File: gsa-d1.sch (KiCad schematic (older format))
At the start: 4 parts, among them J1 CONN-3, SW1 DPST

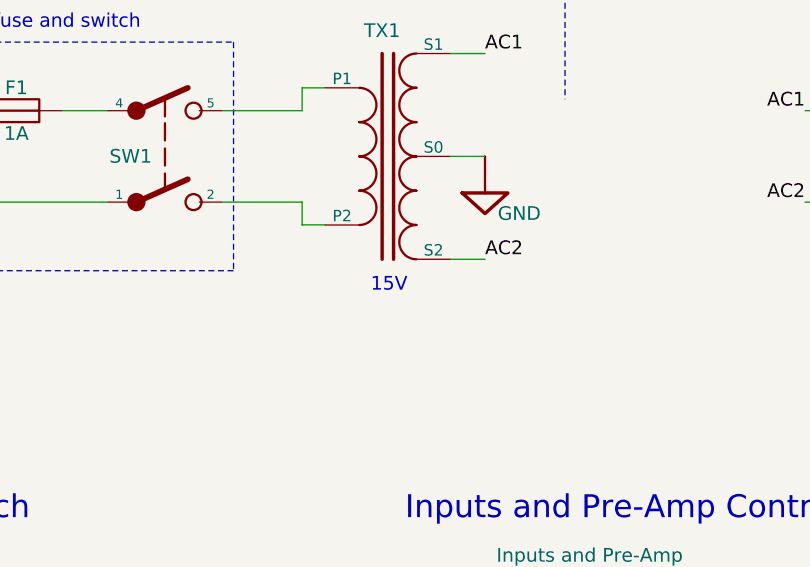
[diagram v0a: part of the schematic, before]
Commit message: Minor layout improvements to pre-amp controls
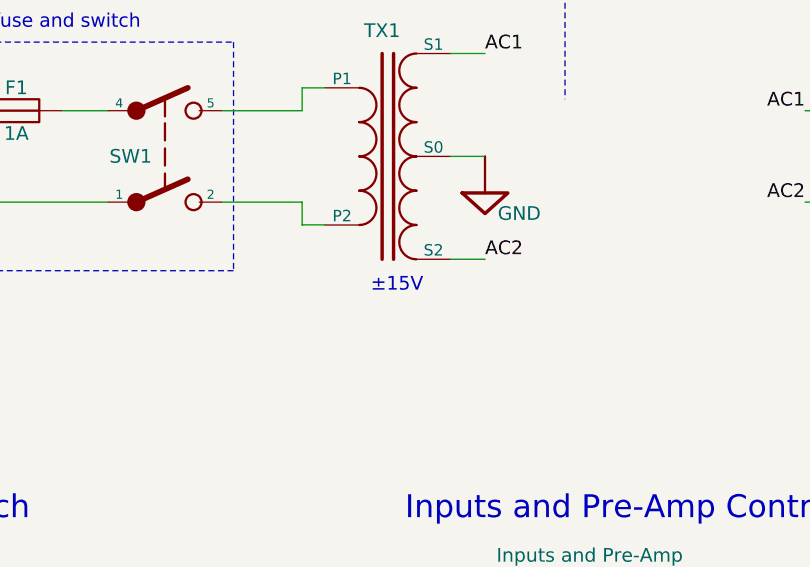
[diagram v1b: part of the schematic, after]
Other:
- note added: "±15V"
- note removed: "15V"
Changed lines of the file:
@@
 EESchema Schematic File Version 2
 LIBS:gsa
+LIBS:gsa-d1-cache
 EELAYER 25 0
 EELAYER END
@@
 AC
 Text Notes 4600 3750 0    60   ~ 0
-15V
+±15V
 $Comp
 L XFRMR-C TX1

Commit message: Updated to use KiCad v5
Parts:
- F1: footprint gsa:NONE -> (none); symbol FUSE -> gsa:FUSE
- J1: footprint gsa:NONE -> (none); symbol CONN-3 -> gsa:CONN-3
- SW1: footprint gsa:NONE -> (none); symbol DPST -> gsa:DPST
- TX1: footprint gsa:NONE -> (none); symbol XFRMR-C -> gsa:XFRMR-C
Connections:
- wire segments 22 -> 23
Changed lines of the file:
@@
-EESchema Schematic File Version 2
+EESchema Schematic File Version 4
 LIBS:gsa
 LIBS:gsa-d1-cache
-EELAYER 25 0
+EELAYER 29 0
 EELAYER END
 $Descr A4 11693 8268
@@
 Sheet 1 5
 Title "Diamond-1"
-Date "January 2018"
+Date "May 2019"
 Rev "2.0.0"
 Comp "Gemstone Amplification"
-Comment1 "© Tim Baldwin 2016,2018"
+Comment1 "© Tim Baldwin 2016,2019"
 Comment2 ""
 Comment3 ""
@@
 	1750 2900 1750 2100
 $Comp
-L CONN-3 J1
+L gsa:CONN-3 J1
 U 1 1 5A85D3B0
 P 2250 3150
 F 0 "J1" H 2250 2850 60  0000 C CNN
 F 1 "CONN-3" H 2250 2875 60  0001 C CNN
-F 2 "gsa:NONE" H 2250 3150 60  0001 C CNN
+F 2 "" H 2250 3150 60  0001 C CNN
 F 3 "" H 2250 3150 60  0000 C CNN
 	1    2250 3150
@@
 ±15V
 $Comp
-L XFRMR-C TX1
+L gsa:XFRMR-C TX1
 U 1 1 5A85D3B4
 P 4700 3150
 F 0 "TX1" H 4650 3700 60  0000 C CNN
 F 1 "XFRMR-C" H 4700 2600 60  0001 C CNN
-F 2 "gsa:NONE" H 5050 2750 60  0001 C CNN
+F 2 "" H 5050 2750 60  0001 C CNN
 F 3 "" H 5050 2750 60  0000 C CNN
 	1    4700 3150
@@
 $EndComp
 $Comp
-L DPST SW1
+L gsa:DPST SW1
 U 1 1 5A85D3B8
 P 3700 3150
 F 0 "SW1" H 3550 3150 60  0000 C CNN
 F 1 "DPST" H 3700 2850 60  0001 C CNN
-F 2 "gsa:NONE" H 3690 3340 60  0001 C CNN
+F 2 "" H 3690 3340 60  0001 C CNN
 F 3 "" H 3690 3340 60  0000 C CNN
 	1    3700 3150
@@
 $EndComp
 $Comp
-L FUSE F1
+L gsa:FUSE F1
 U 1 1 5A85D3B9
 P 3050 2950
 F 0 "F1" H 3050 3050 60  0000 C CNN
 F 1 "1A" H 3050 2850 60  0000 C CNN
-F 2 "gsa:NONE" V 3050 2950 60  0001 C CNN
+F 2 "" V 3050 2950 60  0001 C CNN
 F 3 "" V 3050 2950 60  0000 C CNN
 	1    3050 2950
@@
 	4300 2950 3950 2950
 Wire Wire Line
-	2500 3150 2500 3750
+	2500 3150 2500 3500
 Wire Wire Line
 	2650 3050 2450 3050
@@
 	5450 2100 5450 2900
 $Comp
-L GND #GND01
+L gsa:GND #GND01
 U 1 1 5A85D3CC
 P 5100 3150
@@
 $EndSheet
 $Comp
-L EARTH #GND02
+L gsa:EARTH #GND02
 U 1 1 5A86B538
 P 2500 3750
@@
 Power Supply
 $Comp
-L GND #GND?
+L gsa:GND #GND?
 U 1 1 5A9150C8
 P 2800 3750
@@
 	2800 3500 2500 3500
 Connection ~ 2500 3500
+Wire Wire Line
+	2500 3500 2500 3750
 $EndSCHEMATC

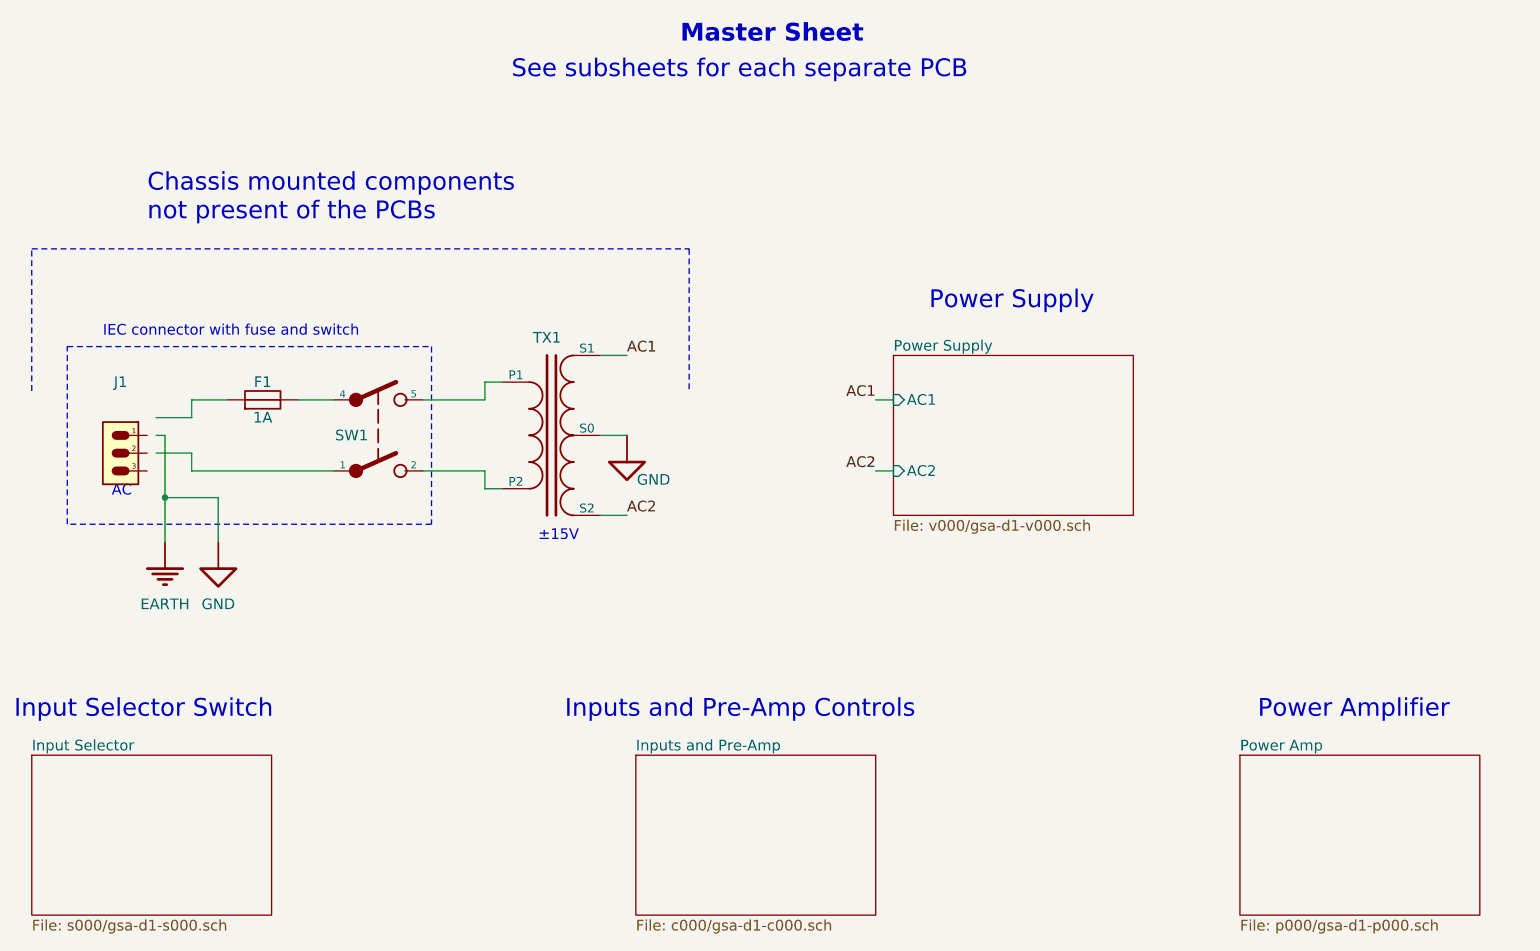
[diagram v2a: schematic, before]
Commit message: Updated to use gsa-lib v1.1
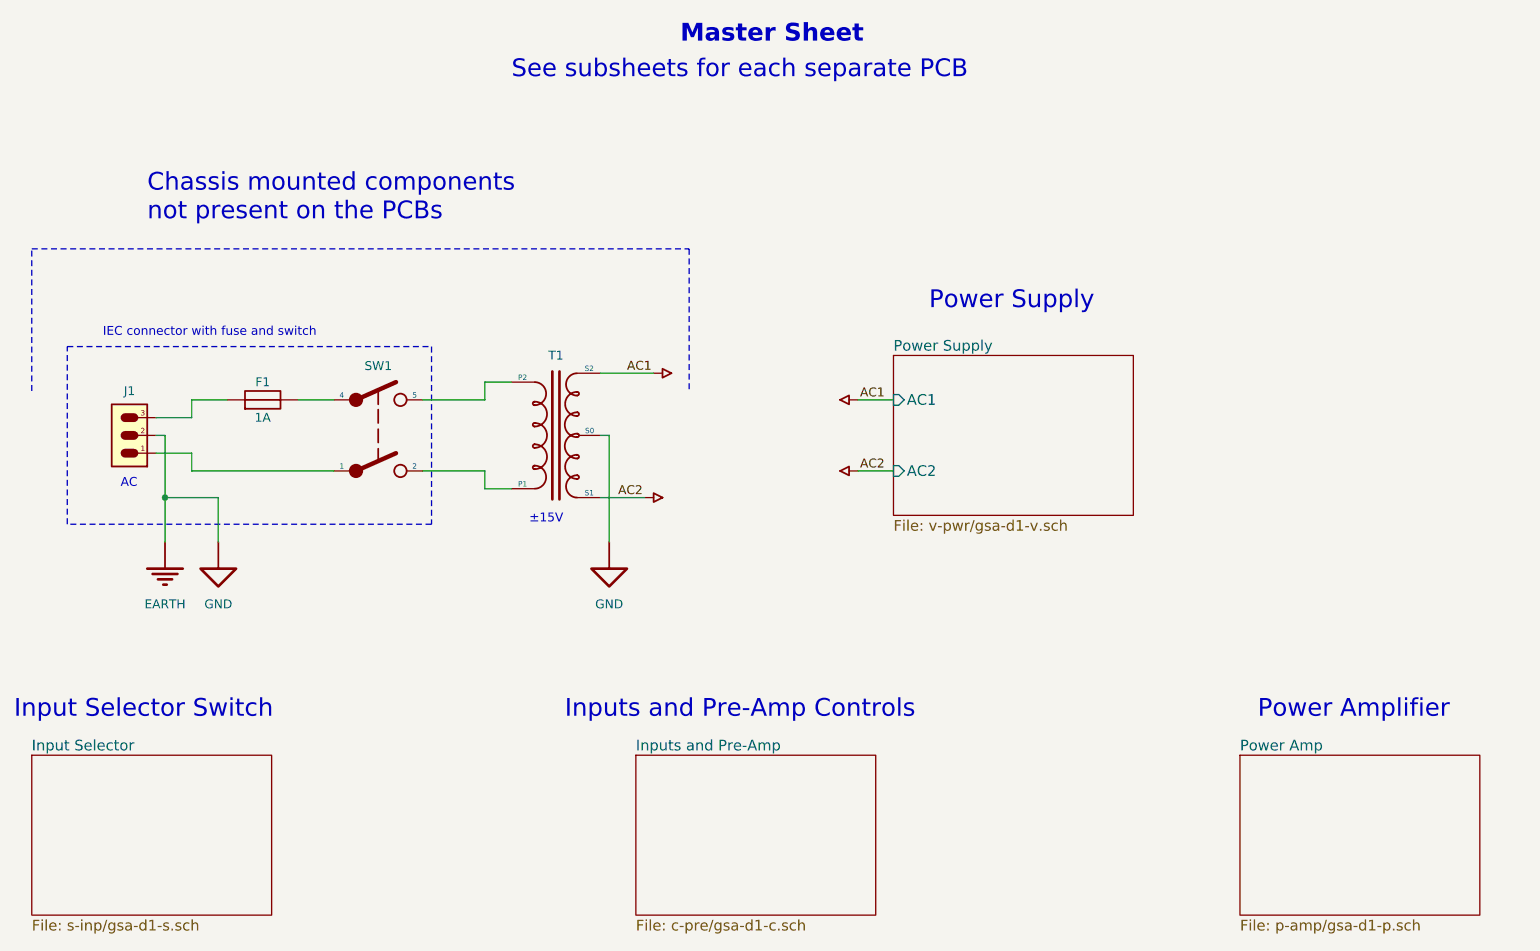
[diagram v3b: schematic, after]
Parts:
- removed SW1: DPST, symbol gsa:DPST
- removed TX1: XFRMR-C, symbol gsa:XFRMR-C
- added SW1: SW-DPST, symbol gsa:SW-DPST
- added T1: XFRMR-CTR, symbol gsa:XFRMR-CTR
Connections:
- wire segments 23 -> 24
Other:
- note added: "Chassis mounted components \nnot present on the PCBs"
- note removed: "Chassis mounted components \nnot present of the PCBs"
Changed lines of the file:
@@
 EESchema Schematic File Version 4
-LIBS:gsa
-LIBS:gsa-d1-cache
-EELAYER 29 0
+EELAYER 30 0
 EELAYER END
 $Descr A4 11693 8268
@@
 Sheet 1 5
 Title "Diamond-1"
-Date "May 2019"
-Rev "2.0.0"
+Date "May 2020"
+Rev "2.0.1"
 Comp "Gemstone Amplification"
-Comment1 "© Tim Baldwin 2016,2019"
-Comment2 ""
+Comment1 "© Tim Baldwin 2016,2020"
+Comment2 "GSA-D1-201"
 Comment3 ""
 Comment4 "Stereo Amplifier"
 $EndDescr
 Text Notes 2400 1950 0    100  ~ 0
-Chassis mounted components \nnot present of the PCBs
+Chassis mounted components \nnot present on the PCBs
 Wire Notes Line
 	1750 2900 1750 2100
-$Comp
-L gsa:CONN-3 J1
-U 1 1 5A85D3B0
-P 2250 3150
-F 0 "J1" H 2250 2850 60  0000 C CNN
-F 1 "CONN-3" H 2250 2875 60  0001 C CNN
-F 2 "" H 2250 3150 60  0001 C CNN
-F 3 "" H 2250 3150 60  0000 C CNN
-	1    2250 3150
-	-1   0    0    1
-$EndComp
-Text Notes 2200 3500 0    60   ~ 0
+Text Notes 2250 3450 0    50   ~ 0
 AC
-Text Notes 4600 3750 0    60   ~ 0
+Text Notes 4550 3650 0    50   ~ 0
 ±15V
-$Comp
-L gsa:XFRMR-C TX1
-U 1 1 5A85D3B4
-P 4700 3150
-F 0 "TX1" H 4650 3700 60  0000 C CNN
-F 1 "XFRMR-C" H 4700 2600 60  0001 C CNN
-F 2 "" H 5050 2750 60  0001 C CNN
-F 3 "" H 5050 2750 60  0000 C CNN
-	1    4700 3150
-	1    0    0    -1
-$EndComp
-$Comp
-L gsa:DPST SW1
-U 1 1 5A85D3B8
-P 3700 3150
-F 0 "SW1" H 3550 3150 60  0000 C CNN
-F 1 "DPST" H 3700 2850 60  0001 C CNN
-F 2 "" H 3690 3340 60  0001 C CNN
-F 3 "" H 3690 3340 60  0000 C CNN
-	1    3700 3150
-	1    0    0    -1
-$EndComp
 $Comp
 L gsa:FUSE F1
 U 1 1 5A85D3B9
 P 3050 2950
-F 0 "F1" H 3050 3050 60  0000 C CNN
-F 1 "1A" H 3050 2850 60  0000 C CNN
-F 2 "" V 3050 2950 60  0001 C CNN
-F 3 "" V 3050 2950 60  0000 C CNN
+F 0 "F1" H 3050 3050 50  0000 C CNN
+F 1 "1A" H 3050 2850 50  0000 C CNN
+F 2 "" V 3050 2950 50  0001 C CNN
+F 3 "" V 3050 2950 50  0001 C CNN
 	1    3050 2950
 	1    0    0    -1
 $EndComp
-Text Notes 2150 2600 0    60   ~ 0
+Text Notes 2150 2600 0    50   ~ 0
 IEC connector with fuse and switch
 Wire Wire Line
-	4950 3600 5100 3600
-Wire Wire Line
-	4950 3150 5100 3150
-Wire Wire Line
-	4950 2700 5100 2700
+	4950 3500 5200 3500
+Wire Wire Line
+	4950 2800 5250 2800
 Wire Wire Line
 	2650 3250 2650 3350
@@
 	2650 2950 2650 3050
 Wire Wire Line
-	4300 3450 4400 3450
+	4300 3450 4450 3450
 Wire Wire Line
 	4300 3350 4300 3450
@@
 	4300 2850 4300 2950
 Wire Wire Line
-	4400 2850 4300 2850
+	4450 2850 4300 2850
 Wire Notes Line
 	1750 2100 5450 2100
 Wire Notes Line
 	5450 2100 5450 2900
-$Comp
-L gsa:GND #GND01
-U 1 1 5A85D3CC
-P 5100 3150
-F 0 "#GND01" H 5240 3070 60  0001 C CNN
-F 1 "GND" H 5250 2900 60  0000 C CNN
-F 2 "" H 5100 2950 60  0000 C CNN
-F 3 "" H 5100 2950 60  0000 C CNN
-	1    5100 3150
-	1    0    0    -1
-$EndComp
 $Sheet
 S 1750 4950 1350 900
 U 5A85D422
 F0 "Input Selector" 60
-F1 "s000/gsa-d1-s000.sch" 60
+F1 "s-inp/gsa-d1-s.sch" 60
 $EndSheet
 $Sheet
@@
 U 5A85D43A
 F0 "Inputs and Pre-Amp" 60
-F1 "c000/gsa-d1-c000.sch" 60
+F1 "c-pre/gsa-d1-c.sch" 60
 $EndSheet
 $Sheet
@@
 U 5A85D452
 F0 "Power Amp" 60
-F1 "p000/gsa-d1-p000.sch" 60
+F1 "p-amp/gsa-d1-p.sch" 60
 $EndSheet
 Text Notes 5400 950  0    100  ~ 20
 Master Sheet
-Text Label 5100 2700 0    60   ~ 0
+Text Label 5100 2800 0    50   ~ 0
 AC1
-Text Label 5100 3600 0    60   ~ 0
+Text Label 5050 3500 0    50   ~ 0
 AC2
-Wire Wire Line
-	6600 2950 6500 2950
-Wire Wire Line
-	6600 3350 6500 3350
-Text Label 6500 2950 2    60   ~ 0
+Text Label 6550 2950 2    50   ~ 0
 AC1
-Text Label 6500 3350 2    60   ~ 0
+Text Label 6550 3350 2    50   ~ 0
 AC2
 $Sheet
@@
 U 5A85D46A
 F0 "Power Supply" 60
-F1 "v000/gsa-d1-v000.sch" 60
+F1 "v-pwr/gsa-d1-v.sch" 60
 F2 "AC1" I L 6600 2950 60
 F3 "AC2" I L 6600 3350 60
@@
 U 1 1 5A86B538
 P 2500 3750
-F 0 "#GND02" H 2640 3670 60  0001 C CNN
-F 1 "EARTH" H 2500 3400 60  0000 C CNN
-F 2 "" H 2500 3550 60  0000 C CNN
-F 3 "" H 2500 3550 60  0000 C CNN
+F 0 "#GND02" H 2640 3670 50  0001 C CNN
+F 1 "EARTH" H 2500 3400 50  0000 C CNN
+F 2 "" H 2500 3550 50  0001 C CNN
+F 3 "" H 2500 3550 50  0001 C CNN
 	1    2500 3750
 	1    0    0    -1
@@
 Power Supply
 $Comp
-L gsa:GND #GND?
+L gsa:GND #GND0101
 U 1 1 5A9150C8
 P 2800 3750
-F 0 "#GND?" H 2940 3670 60  0001 C CNN
-F 1 "GND" H 2800 3400 60  0000 C CNN
-F 2 "" H 2800 3550 60  0000 C CNN
-F 3 "" H 2800 3550 60  0000 C CNN
+F 0 "#GND0101" H 2940 3670 50  0001 C CNN
+F 1 "GND" H 2800 3400 50  0000 C CNN
+F 2 "" H 2800 3550 50  0001 C CNN
+F 3 "" H 2800 3550 50  0001 C CNN
 	1    2800 3750
 	1    0    0    -1
@@
 Wire Wire Line
 	2500 3500 2500 3750
+$Comp
+L gsa:SW-DPST SW1
+U 1 1 5EB824D8
+P 3700 3150
+F 0 "SW1" H 3700 3541 50  0000 C CNN
+F 1 "SW-DPST" H 3700 3550 50  0001 C CNN
+F 2 "" H 3690 3340 50  0001 C CNN
+F 3 "" H 3690 3340 50  0001 C CNN
+	1    3700 3150
+	1    0    0    -1
+$EndComp
+$Comp
+L gsa:XFRMR-CTR T1
+U 1 1 5EC0B1E2
+P 4700 3150
+F 0 "T1" H 4700 3600 50  0000 C CNN
+F 1 "XFRMR-CTR" H 4725 2600 50  0001 C CNN
+F 2 "" H 5075 2750 50  0001 C CNN
+F 3 "" H 5075 2750 50  0001 C CNN
+	1    4700 3150
+	1    0    0    -1
+$EndComp
+$Comp
+L gsa:CONN-3 J1
+U 1 1 5EC10A81
+P 2300 3250
+F 0 "J1" H 2300 3600 50  0000 C CNN
+F 1 "CONN-3" H 2300 2975 50  0001 C CNN
+F 2 "" H 2300 3250 50  0001 C CNN
+F 3 "" H 2300 3250 50  0001 C CNN
+	1    2300 3250
+	-1   0    0    -1
+$EndComp
+$Comp
+L gsa:NET #SYM102
+U 1 1 5EF6D9D7
+P 5250 3500
+F 0 "#SYM102" H 5250 3600 50  0001 C CNN
+F 1 "NET" H 5243 3608 50  0001 C CNN
+F 2 "" H 5250 3500 50  0001 C CNN
+F 3 "" H 5250 3500 50  0001 C CNN
+	1    5250 3500
+	1    0    0    -1
+$EndComp
+$Comp
+L gsa:NET #SYM101
+U 1 1 5EF6DDA5
+P 5300 2800
+F 0 "#SYM101" H 5300 2900 50  0001 C CNN
+F 1 "NET" H 5300 2050 50  0001 C CNN
+F 2 "" H 5300 2800 50  0001 C CNN
+F 3 "" H 5300 2800 50  0001 C CNN
+	1    5300 2800
+	1    0    0    -1
+$EndComp
+$Comp
+L gsa:NET #SYM103
+U 1 1 5EF7160D
+P 6350 2950
+F 0 "#SYM103" H 6350 3050 50  0001 C CNN
+F 1 "NET" H 6350 2850 50  0001 C CNN
+F 2 "" H 6350 2950 50  0001 C CNN
+F 3 "" H 6350 2950 50  0001 C CNN
+	1    6350 2950
+	-1   0    0    1
+$EndComp
+$Comp
+L gsa:NET #SYM104
+U 1 1 5EF71C7E
+P 6350 3350
+F 0 "#SYM104" H 6350 3450 50  0001 C CNN
+F 1 "NET" H 6350 3250 50  0001 C CNN
+F 2 "" H 6350 3350 50  0001 C CNN
+F 3 "" H 6350 3350 50  0001 C CNN
+	1    6350 3350
+	-1   0    0    1
+$EndComp
+Wire Wire Line
+	6400 2950 6600 2950
+Wire Wire Line
+	6400 3350 6600 3350
+$Comp
+L gsa:GND #GND01
+U 1 1 5A85D3CC
+P 5000 3750
+F 0 "#GND01" H 5140 3670 50  0001 C CNN
+F 1 "GND" H 5000 3400 50  0000 C CNN
+F 2 "" H 5000 3550 50  0001 C CNN
+F 3 "" H 5000 3550 50  0001 C CNN
+	1    5000 3750
+	1    0    0    -1
+$EndComp
+Wire Wire Line
+	5000 3750 5000 3150
+Wire Wire Line
+	5000 3150 4950 3150
 $EndSCHEMATC
